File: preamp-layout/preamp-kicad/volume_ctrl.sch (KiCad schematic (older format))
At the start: 61 parts, among them J68 Conn_01x02_Male, J69 Conn_01x02_Female, J70 Conn_01x03_Female, J71 Conn_01x03_Female, J72 Conn_01x03_Male, J73 Conn_01x03_Male, J74 Conn_01x03_Female, U20 MCP4902, U21 MCP4902, U22 TL072, U23 TL072, U24 THAT2181, U25 THAT2181, U26 TL072, U27 THAT2181, U28 THAT2181, U29 TL072

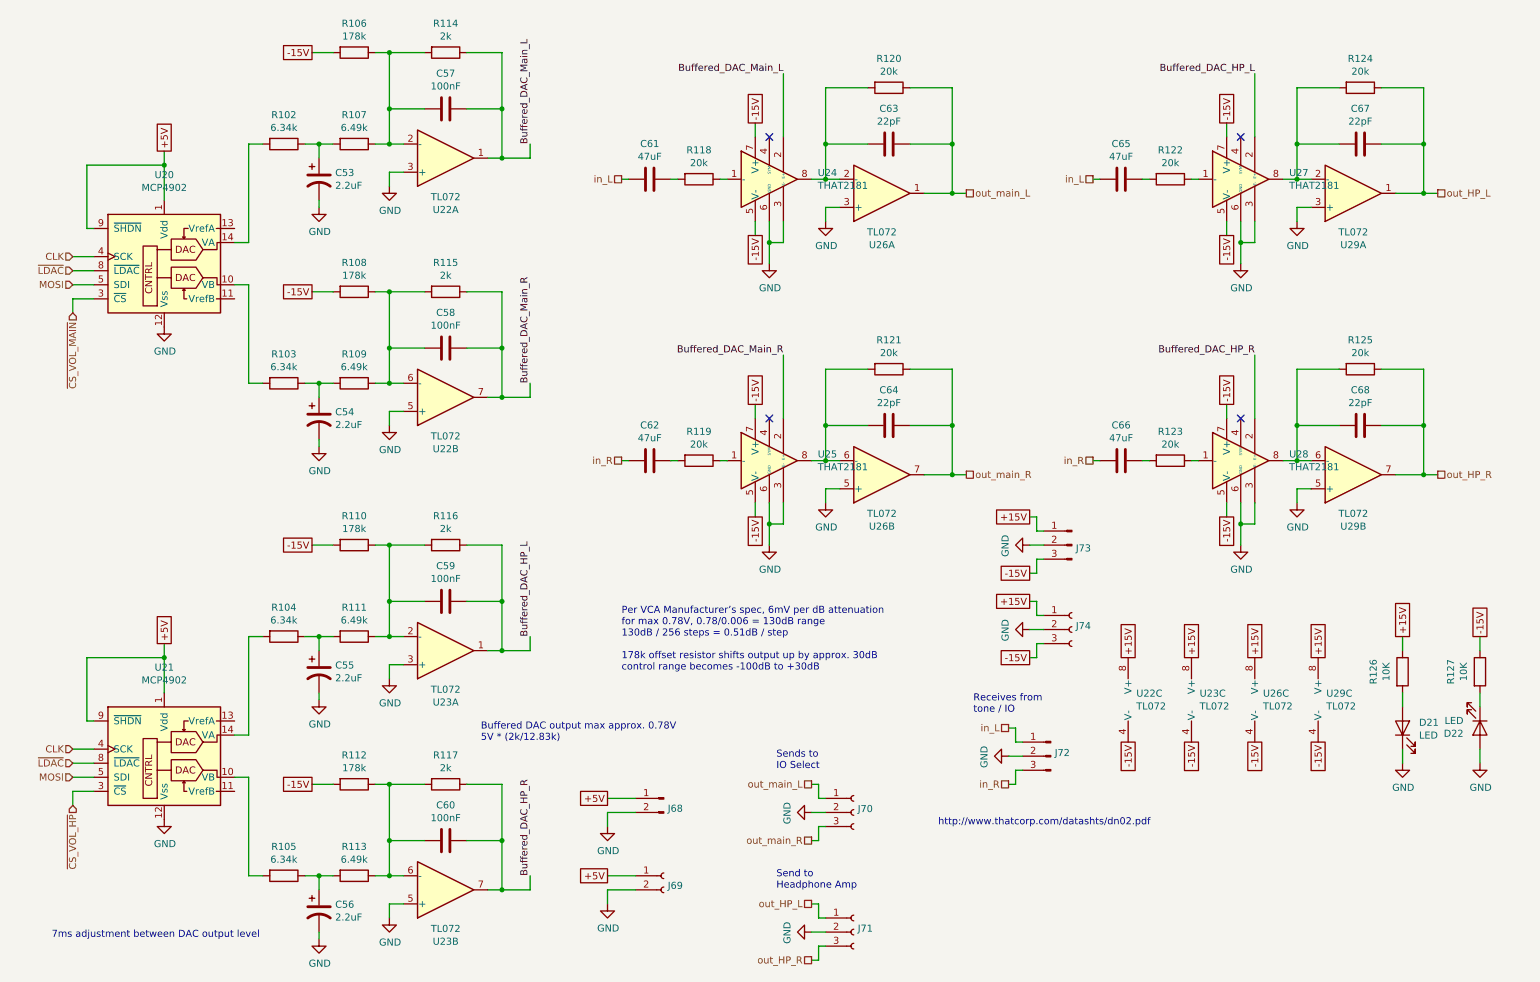
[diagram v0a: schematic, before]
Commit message: AC PCB Update
Removed Switch symbol from PCB, moved to main sheet. Started playing with footprint assignment. Other minor updates.
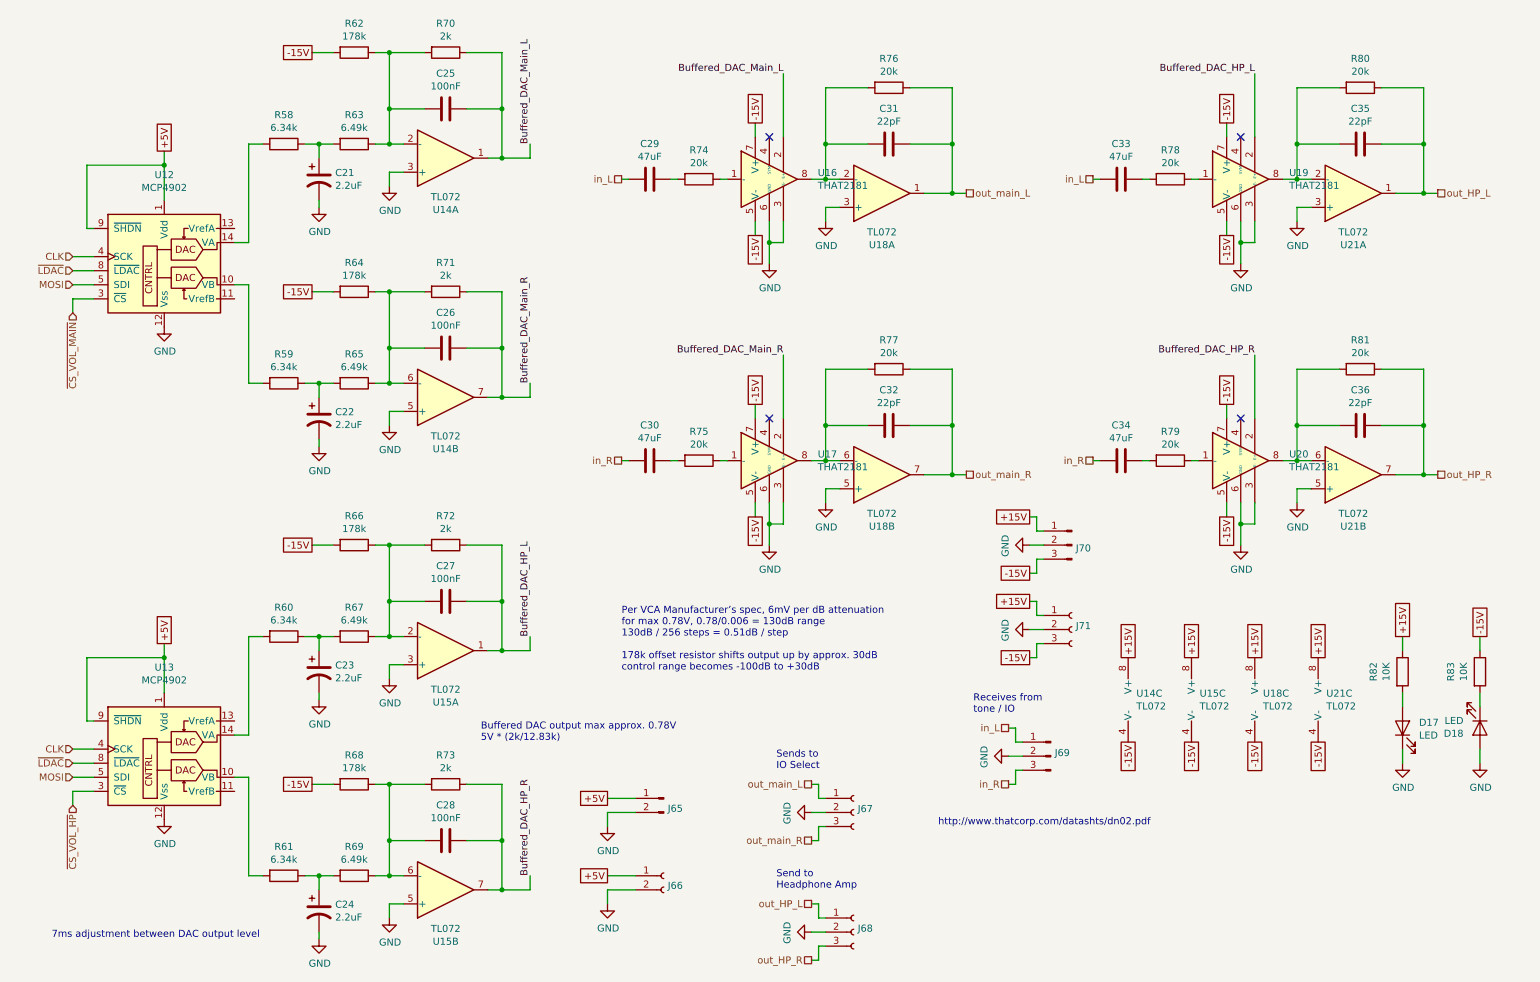
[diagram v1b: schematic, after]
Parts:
- renumbered C53 to C21, C54 to C22, C55 to C23, C56 to C24, C57 to C25, C58 to C26, C59 to C27, C60 to C28, C61 to C29, C62 to C30, C63 to C31, C64 to C32, C65 to C33, C66 to C34, C67 to C35, C68 to C36, D21 to D17, D22 to D18, J68 to J65, J69 to J66, J70 to J67, J71 to J68, J72 to J69, J73 to J70, J74 to J71, R102 to R58, R103 to R59, R104 to R60, R105 to R61, R106 to R62, R107 to R63, R108 to R64, R109 to R65, R110 to R66, R111 to R67, R112 to R68, R113 to R69, R114 to R70, R115 to R71, R116 to R72, R117 to R73, R118 to R74, R119 to R75, R120 to R76, R121 to R77, R122 to R78, R123 to R79, R124 to R80, R125 to R81, R126 to R82, R127 to R83, U20 to U12, U21 to U13, U22 to U14, U23 to U15, U24 to U16, U25 to U17, U26 to U18, U27 to U19, U28 to U20, U29 to U21

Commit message: Initial Footprint Assignment
Assigned footprints to SMT resistors, pin headers, screw terminals, LEDs, DIP-8 ICs
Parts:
- D17, D18: footprint (none) -> LED_SMD:LED_1206_3216Metric_Pad1.42x1.75mm_HandSolder
- J65, J66: footprint (none) -> Connector_PinHeader_2.54mm:PinHeader_1x02_P2.54mm_Vertical
- J67, J68, J69, J70, J71: footprint (none) -> Connector_PinHeader_2.54mm:PinHeader_1x03_P2.54mm_Vertical
- R58, R59, R60, R61, R63, R64, R65, R66, R67, R68, R69, R70, R71, R72, R73, R74, R75, R76, R77, R78, R79, R80, R81, R82, R83: footprint (none) -> Resistor_SMD:R_1206_3216Metric_Pad1.42x1.75mm_HandSolder
- R62: footprint (none) -> Resistor_SMD:R_1206_3216Metric_Pad1.42x1.75mm_HandSolderv
- U14, U15, U18, U21: footprint (none) -> Package_DIP:DIP-8_W7.62mm_Socket_LongPads

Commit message: BOM update
Minor changes to schematic, value changes and footprint entry. BOM updated with parts sourcing
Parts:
- added D21: LED, LED_SMD:LED_1206_3216Metric_Pad1.42x1.75mm_HandSolder, symbol Device:LED
- added R86: 430, Resistor_SMD:R_1206_3216Metric_Pad1.42x1.75mm_HandSolder, symbol Device:R
- R82, R83: value 10K -> 430
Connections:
- net +5V: now also R86.1
- net GND: now also D21.1 (K)
- new net: D21.2 (A), R86.2
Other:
- note added: "7ms adjustment\nbetween DAC output level"
- note added: "Buffered DAC output max approx. 0.78V\n5V * (2k/(6.34k+6.49k))"
- note removed: "7ms adjustment between DAC output level"
- note removed: "Buffered DAC output max approx. 0.78V\n5V * (2k/12.83k)"
- moved on the sheet: D17, D18, J69, J70, J71, R82, R83, U14C, U15C, U18C, U21C

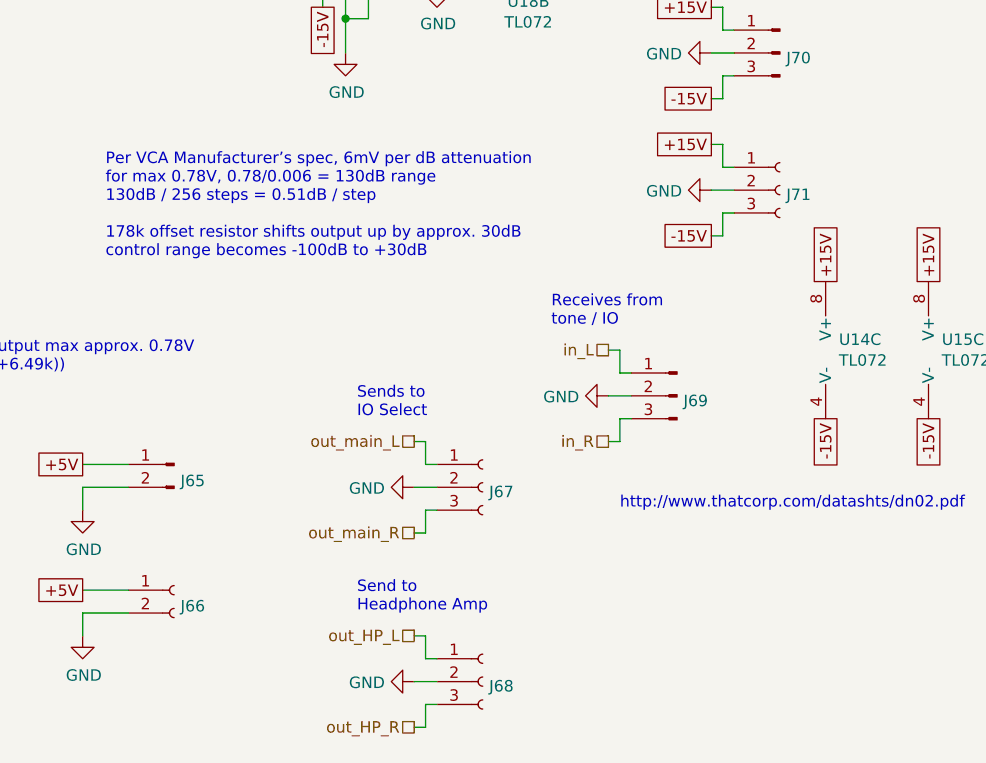
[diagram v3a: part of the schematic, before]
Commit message: power headers updated, slight BOM update
changed footprint on all 5V, +-15V to JST B2B / B3B connectors. All male conns now.
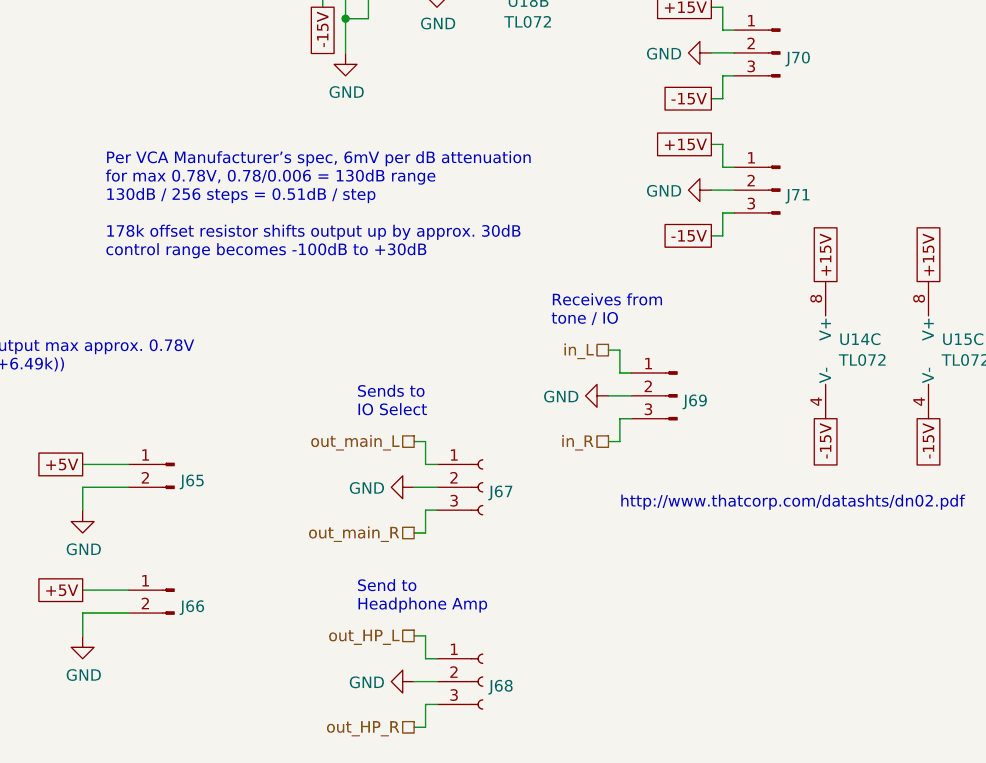
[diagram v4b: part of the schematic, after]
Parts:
- removed J66: Conn_01x02_Female, Connector_PinHeader_2.54mm:PinHeader_1x02_P2.54mm_Vertical, symbol Connector:Conn_01x02_Female
- removed J71: Conn_01x03_Female, Connector_PinHeader_2.54mm:PinHeader_1x03_P2.54mm_Vertical, symbol Connector:Conn_01x03_Female
- added J66: Conn_01x02_Male, Connector_JST:JST_EH_B2B-EH-A_1x02_P2.50mm_Vertical, symbol Connector:Conn_01x02_Male
- added J71: Conn_01x03_Male, Connector_JST:JST_EH_B3B-EH-A_1x03_P2.50mm_Vertical, symbol Connector:Conn_01x03_Male
- J65: footprint Connector_PinHeader_2.54mm:PinHeader_1x02_P2.54mm_Vertical -> Connector_JST:JST_EH_B2B-EH-A_1x02_P2.50mm_Vertical
- J70: footprint Connector_PinHeader_2.54mm:PinHeader_1x03_P2.54mm_Vertical -> Connector_JST:JST_EH_B3B-EH-A_1x03_P2.50mm_Vertical
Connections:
- net +15V: now also J71.1 (Pin_1)
- net +5V: now also J66.1 (Pin_1)
- net -15V: now also J71.3 (Pin_3)
- net GND: now also J66.2 (Pin_2), J71.2 (Pin_2)
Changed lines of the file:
@@
 F 0 "J70" H 7672 4478 50  0000 R CNN
 F 1 "Conn_01x03_Male" H 7672 4433 50  0001 R CNN
-F 2 "Connector_PinHeader_2.54mm:PinHeader_1x03_P2.54mm_Vertical" H 7700 4500 50  0001 C CNN
+F 2 "Connector_JST:JST_EH_B3B-EH-A_1x03_P2.50mm_Vertical" H 7700 4500 50  0001 C CNN
 F 3 "~" H 7700 4500 50  0001 C CNN
 	1    7700 4500
@@
 F 0 "J65" H 5022 6228 50  0000 R CNN
 F 1 "Conn_01x02_Male" H 5022 6183 50  0001 R CNN
-F 2 "Connector_PinHeader_2.54mm:PinHeader_1x02_P2.54mm_Vertical" H 5050 6300 50  0001 C CNN
+F 2 "Connector_JST:JST_EH_B2B-EH-A_1x02_P2.50mm_Vertical" H 5050 6300 50  0001 C CNN
 F 3 "~" H 5050 6300 50  0001 C CNN
 	1    5050 6300
@@
 Wire Wire Line
 	4850 6850 4650 6850
-$Comp
-L Connector:Conn_01x03_Female J?
-U 1 1 60B225EE
-P 7700 5100
-AR Path="/5E607732/60B225EE" Ref="J?"  Part="1"
-AR Path="/5E2D8DA2/60B225EE" Ref="J?"  Part="1"
-AR Path="/6009D432/60B225EE" Ref="J71"  Part="1"
-F 0 "J71" H 7728 5080 50  0000 L CNN
-F 1 "Conn_01x03_Female" H 7728 5035 50  0001 L CNN
-F 2 "Connector_PinHeader_2.54mm:PinHeader_1x03_P2.54mm_Vertical" H 7700 5100 50  0001 C CNN
-F 3 "~" H 7700 5100 50  0001 C CNN
-	1    7700 5100
-	1    0    0    -1
-$EndComp
-$Comp
-L Connector:Conn_01x02_Female J66
-U 1 1 60B321C7
-P 5050 6850
-F 0 "J66" H 5078 6780 50  0000 L CNN
-F 1 "Conn_01x02_Female" H 5078 6735 50  0001 L CNN
-F 2 "Connector_PinHeader_2.54mm:PinHeader_1x02_P2.54mm_Vertical" H 5050 6850 50  0001 C CNN
-F 3 "~" H 5050 6850 50  0001 C CNN
-	1    5050 6850
-	1    0    0    -1
-$EndComp
 Wire Wire Line
 	6100 6200 6150 6200
@@
 Text GLabel 10900 5350 1    50   UnSpc ~ 0
 +5V
+$Comp
+L Connector:Conn_01x02_Male J?
+U 1 1 5E6051C6
+P 5050 6850
+AR Path="/5E5EF2D4/5E6051C6" Ref="J?"  Part="1"
+AR Path="/6009D432/5E6051C6" Ref="J66"  Part="1"
+F 0 "J66" H 5022 6778 50  0000 R CNN
+F 1 "Conn_01x02_Male" H 5022 6733 50  0001 R CNN
+F 2 "Connector_JST:JST_EH_B2B-EH-A_1x02_P2.50mm_Vertical" H 5050 6850 50  0001 C CNN
+F 3 "~" H 5050 6850 50  0001 C CNN
+	1    5050 6850
+	-1   0    0    -1
+$EndComp
+$Comp
+L Connector:Conn_01x03_Male J?
+U 1 1 5E62BFCF
+P 7700 5100
+AR Path="/5E27B612/5E62BFCF" Ref="J?"  Part="1"
+AR Path="/6009D432/5E62BFCF" Ref="J71"  Part="1"
+F 0 "J71" H 7672 5078 50  0000 R CNN
+F 1 "Conn_01x03_Male" H 7672 5033 50  0001 R CNN
+F 2 "Connector_JST:JST_EH_B3B-EH-A_1x03_P2.50mm_Vertical" H 7700 5100 50  0001 C CNN
+F 3 "~" H 7700 5100 50  0001 C CNN
+	1    7700 5100
+	-1   0    0    -1
+$EndComp
 $EndSCHEMATC

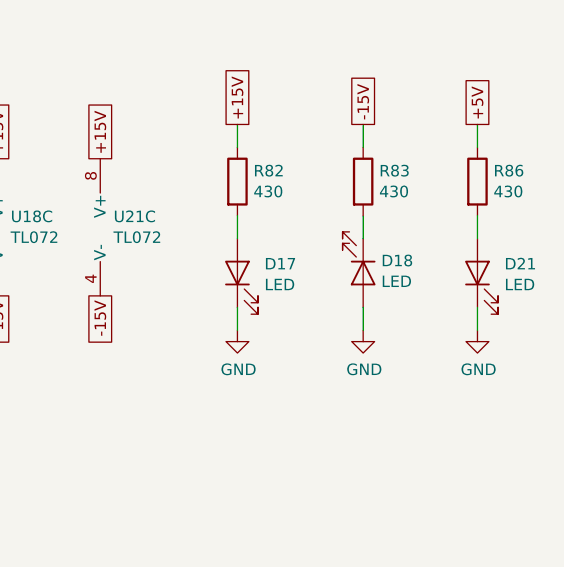
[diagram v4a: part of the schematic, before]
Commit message: Added front panel LED sheet. BOM update. Front panel PCA work
other minor changes like LED color assignments, etc
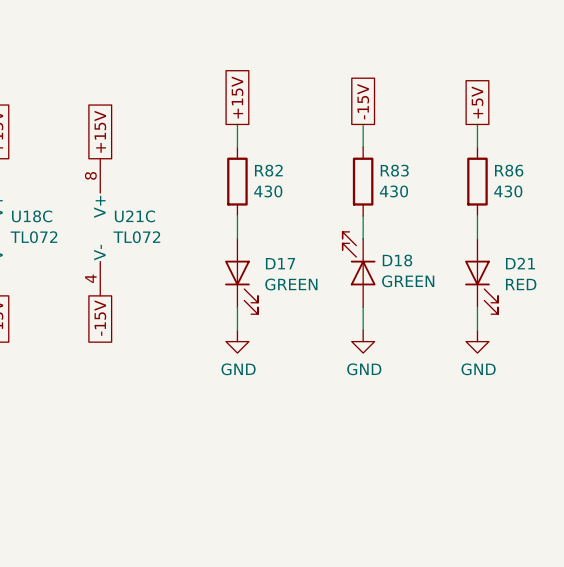
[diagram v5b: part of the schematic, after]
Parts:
- D17, D18: value LED -> GREEN
- D21: value LED -> RED
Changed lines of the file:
@@
 $Descr A4 11693 8268
 encoding utf-8
-Sheet 11 11
+Sheet 11 12
 Title ""
 Date "2020-01-23"
@@
 AR Path="/6009D432/6072D503" Ref="D17"  Part="1"
 F 0 "D17" V 9889 5882 50  0000 R CNN
-F 1 "LED" V 9798 5882 50  0000 R CNN
+F 1 "GREEN" V 9798 5882 50  0000 R CNN
 F 2 "LED_SMD:LED_1206_3216Metric_Pad1.42x1.75mm_HandSolder" H 9850 6000 50  0001 C CNN
 F 3 "~" H 9850 6000 50  0001 C CNN
@@
 AR Path="/6009D432/6072D513" Ref="D18"  Part="1"
 F 0 "D18" V 10347 6079 50  0000 L CNN
-F 1 "LED" V 10438 6079 50  0000 L CNN
+F 1 "GREEN" V 10438 6079 50  0000 L CNN
 F 2 "LED_SMD:LED_1206_3216Metric_Pad1.42x1.75mm_HandSolder" H 10400 6000 50  0001 C CNN
 F 3 "~" H 10400 6000 50  0001 C CNN
@@
 AR Path="/6009D432/5E3D5CEF" Ref="D21"  Part="1"
 F 0 "D21" V 10939 5882 50  0000 R CNN
-F 1 "LED" V 10848 5882 50  0000 R CNN
+F 1 "RED" V 10848 5882 50  0000 R CNN
 F 2 "LED_SMD:LED_1206_3216Metric_Pad1.42x1.75mm_HandSolder" H 10900 6000 50  0001 C CNN
 F 3 "~" H 10900 6000 50  0001 C CNN

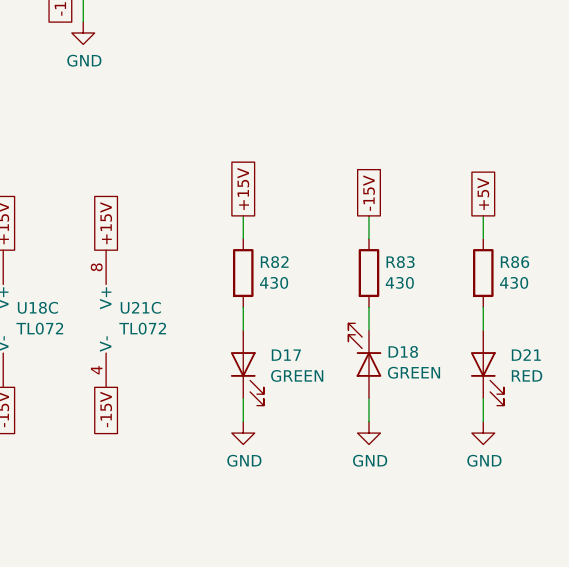
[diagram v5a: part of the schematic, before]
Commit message: LED resistor update
In the process of reviewing layouts and associated parts sourcing, I realized that I had incorrectly calculated the resistors needed for the power supply LEDs on all boards. Updated BOM and schematics to match. Other minor schematic updates.
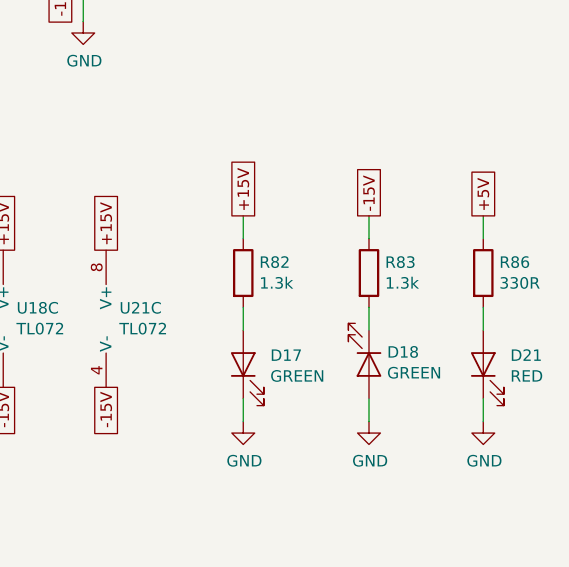
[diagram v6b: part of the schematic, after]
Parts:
- R82, R83: value 430 -> 1.3k
- R86: value 430 -> 330R
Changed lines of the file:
@@
 AR Path="/6009D432/6072D4FD" Ref="R82"  Part="1"
 F 0 "R82" H 9920 5646 50  0000 L CNN
-F 1 "430" H 9920 5555 50  0000 L CNN
+F 1 "1.3k" H 9920 5555 50  0000 L CNN
 F 2 "Resistor_SMD:R_1206_3216Metric_Pad1.42x1.75mm_HandSolder" V 9780 5600 50  0001 C CNN
 F 3 "~" H 9850 5600 50  0001 C CNN
@@
 AR Path="/6009D432/6072D50D" Ref="R83"  Part="1"
 F 0 "R83" H 10470 5646 50  0000 L CNN
-F 1 "430" H 10470 5555 50  0000 L CNN
+F 1 "1.3k" H 10470 5555 50  0000 L CNN
 F 2 "Resistor_SMD:R_1206_3216Metric_Pad1.42x1.75mm_HandSolder" V 10330 5600 50  0001 C CNN
 F 3 "~" H 10400 5600 50  0001 C CNN
@@
 AR Path="/6009D432/5E3D5CE9" Ref="R86"  Part="1"
 F 0 "R86" H 10970 5646 50  0000 L CNN
-F 1 "430" H 10970 5555 50  0000 L CNN
+F 1 "330R" H 10970 5555 50  0000 L CNN
 F 2 "Resistor_SMD:R_1206_3216Metric_Pad1.42x1.75mm_HandSolder" V 10830 5600 50  0001 C CNN
 F 3 "~" H 10900 5600 50  0001 C CNN
